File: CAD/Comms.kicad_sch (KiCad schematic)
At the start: 83 parts, among them J27 uSD_Socket, J43 USB, J46 ETHERNET, Q1 BC807, U13 MCP2542, U15 MCP2542, U16 KSZ8081RNACA, U17 74LVC2G125, U19 74LVC2G34, U3 EMIF06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

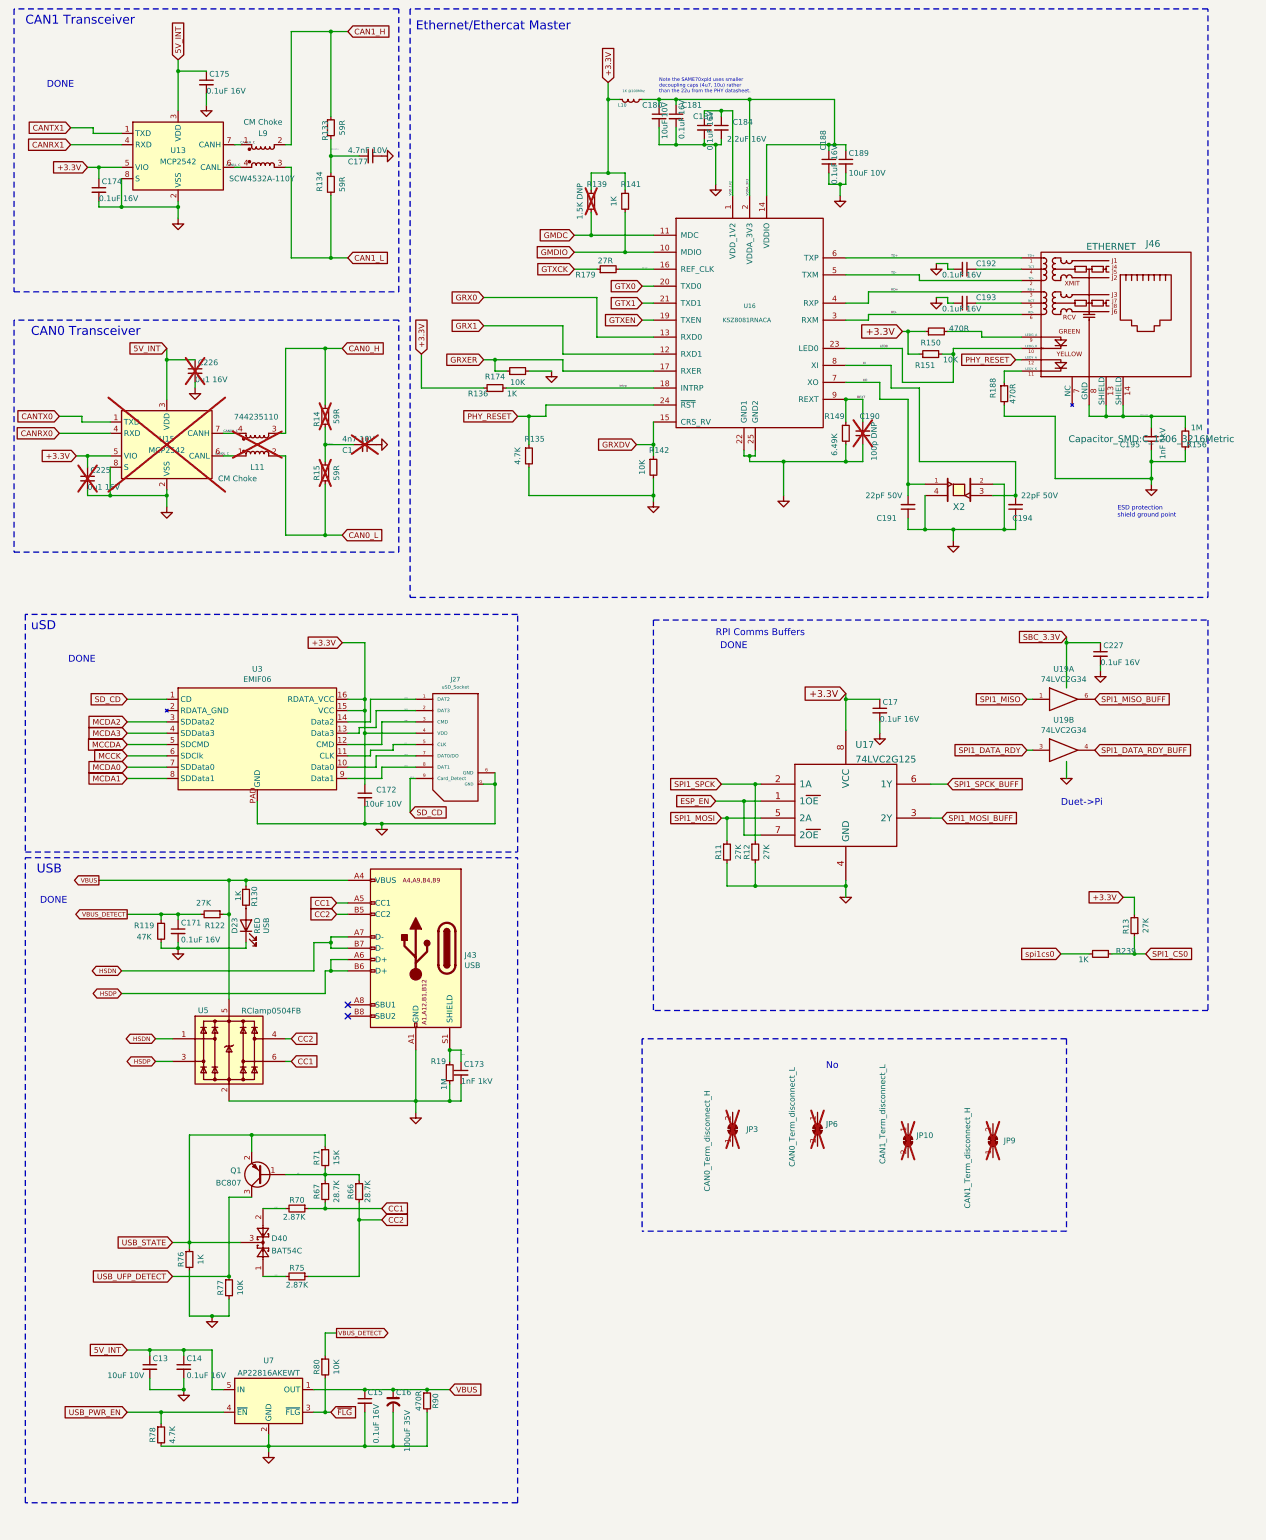
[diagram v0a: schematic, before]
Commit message: WIP redoing board for new print
Removed version resistors.
Added pull-up on CMD.
Working on motors, not routed.
Added local library for custom parts.
Ran auto-cleanup of traces and vias (supervised).
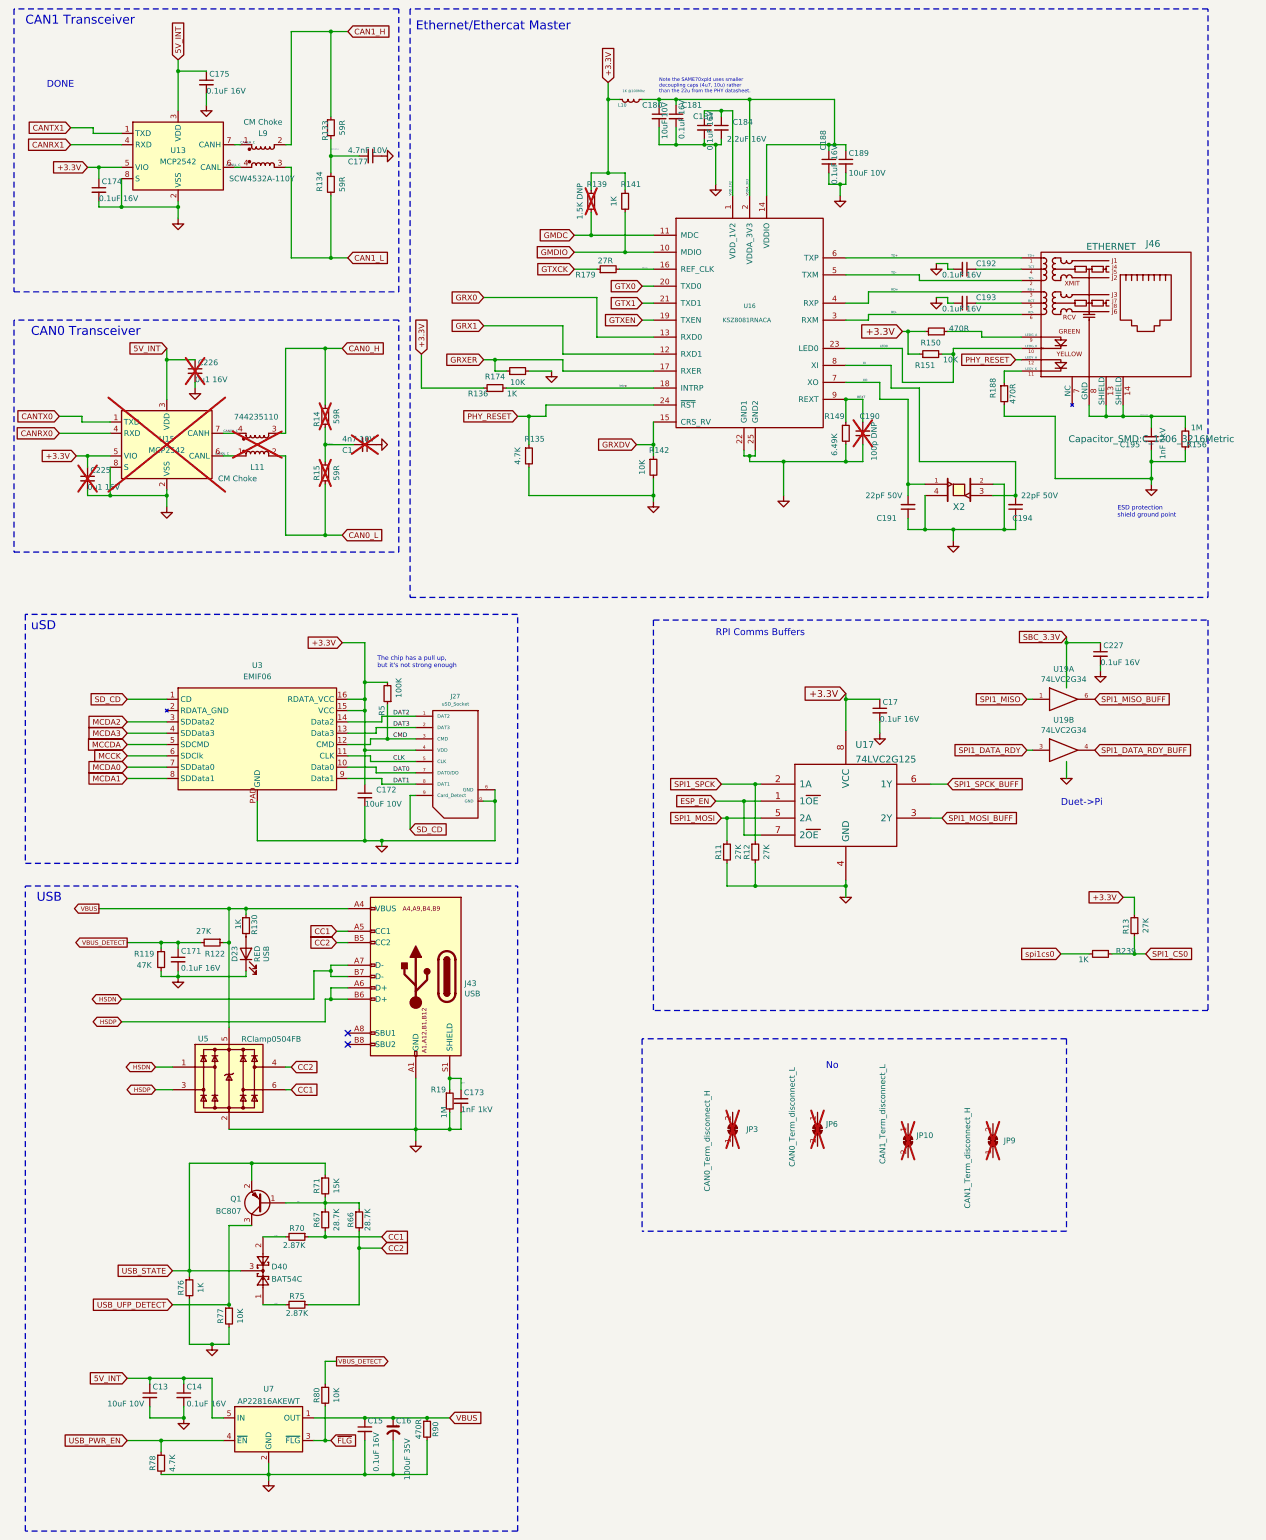
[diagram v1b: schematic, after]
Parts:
- removed U3: EMIF06, Carters_Various_Bits_and_Pieces:QFN-16L-3.5x1.2mm_P0.4mm, symbol Duet3:CM1624
- added R5: 100K, Resistor_SMD:R_0402_1005Metric, symbol Device:R_Small
- added U3: EMIF06, 3DPotter:QFN-16L-3.5x1.2mm_P0.4mm, symbol 3DPotter:EMIF06
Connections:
- net +3.3V: now also R5.2, U3.15 (VCC), U3.16 (RDATA_VCC)
- net CLK: now also U3.11 (CLK)
- net CMD: now also R5.1, U3.12 (CMD)
- net DAT0: now also U3.10 (Data0)
- net DAT1: now also U3.9 (Data1)
- net DAT2: now also U3.14 (Data2)
- net DAT3: now also U3.13 (Data3)
- net GND: now also U3.PAD (GND)
- net MCCDA: now also U3.5 (SDCMD)
- net MCCK: now also U3.6 (SDClk)
- net MCDA0: now also U3.7 (SDData0)
- net MCDA1: now also U3.8 (SDData1)
- net MCDA2: now also U3.3 (SDData2)
- net MCDA3: now also U3.4 (SDData3)
- net SD_CD: now also U3.1 (CD)
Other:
- note added: "The chip has a pull up, but it's not strong enough"
- company: Duet3d -> 3DPotter
- title: Duet 3 Main Board 6XD -> Duet 3 Main Board 3DP
- moved on the sheet: C13, C14, C15, C16, C171, C173, D23, D40, J27, J43, Q1, R119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

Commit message: update led resistors
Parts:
- R130: value 1K -> 845R; LCSC C144789 -> C227247; Part Number AC0402FR-071KL -> AC0402FR-07845RL
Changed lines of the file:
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@@
 			)
 		)
-		(property "Value" "1K"
+		(property "Value" "845R"
 			(at 65.5828 220.6752 90)
 			(effects
@@
 			)
 		)
-		(property "Part Number" "AC0402FR-071KL"
+		(property "Part Number" "AC0402FR-07845RL"
 			(at 67.31 220.98 0)
 			(effects
@@
 			)
 		)
-		(property "LCSC" "C144789"
+		(property "LCSC" "C227247"
 			(at 67.31 220.98 90)
 			(effects

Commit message: Moved Traces and Final Prep before Batch 2
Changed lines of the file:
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@@
 		)
 		(property "Footprint" "Capacitor_SMD:C_1206_3216Metric"
-			(at 270.51 111.76 0)
+			(at 270.256 114.808 0)
 			(effects
 				(font
 					(size 1.524 1.524)
 				)
+				(hide yes)
 			)
 		)

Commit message: QOL
Added a buttload of 3d models, 3d model of board is now usable. Also saved a lot of missing symbols and footprints, which are available in the 3DPotter Library.
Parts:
- J27: footprint complib:uSD_SKT -> 3DPotter:uSD_SKT; symbol Duet3:uSD_Socket -> 3DPotter:uSD_Socket
- J43: footprint complib:USB_C_Receptacle_Valcon_CSP-USC16-TR -> 3DPotter:USB_C_Receptacle_Valcon_CSP-USC16-TR; symbol Duet3:USB_C_Receptacle_USB2.0_16pin -> 3DPotter:USB_C_Receptacle_USB2.0_16pin
- J46: footprint complib:RJ45+MAG -> 3DPotter:RJ45+MAG; symbol Duet3:RJ45+MAG -> 3DPotter:RJ45+MAG
- U16: symbol Duet3:KSZ8081RNACA -> 3DPotter:KSZ8081RNACA
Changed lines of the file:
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@@
 	)
 	(symbol
-		(lib_id "Duet3:KSZ8081RNACA")
+		(lib_id "3DPotter:KSZ8081RNACA")
 		(at 180.34 86.36 0)
 		(unit 1)
@@
 	)
 	(symbol
-		(lib_id "Duet3:uSD_Socket")
+		(lib_id "3DPotter:uSD_Socket")
 		(at 113.03 185.42 0)
 		(unit 1)
@@
 			)
 		)
-		(property "Footprint" "complib:uSD_SKT"
+		(property "Footprint" "3DPotter:uSD_SKT"
 			(at 114.3 170.6626 0)
 			(effects
@@
 	)
 	(symbol
-		(lib_id "Duet3:RJ45+MAG")
+		(lib_id "3DPotter:RJ45+MAG")
 		(at 257.81 83.82 0)
 		(unit 1)
@@
 			)
 		)
-		(property "Footprint" "complib:RJ45+MAG"
+		(property "Footprint" "3DPotter:RJ45+MAG"
 			(at 280.1112 89.8398 0)
 			(effects
@@
 	)
 	(symbol
-		(lib_id "Duet3:USB_C_Receptacle_USB2.0_16pin")
+		(lib_id "3DPotter:USB_C_Receptacle_USB2.0_16pin")
 		(at 105.41 232.41 0)
 		(mirror y)
@@
 			)
 		)
-		(property "Footprint" "complib:USB_C_Receptacle_Valcon_CSP-USC16-TR"
+		(property "Footprint" "3DPotter:USB_C_Receptacle_Valcon_CSP-USC16-TR"
 			(at 101.6 232.41 0)
 			(effects

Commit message: Misc Resistor changes
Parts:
- R130: value 845R -> 5K; LCSC C227247 -> C477765; Part Number AC0402FR-07845RL -> RC0402FR-075KL
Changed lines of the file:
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@@
 			)
 		)
-		(property "Value" "845R"
+		(property "Value" "5K"
 			(at 65.5828 220.6752 90)
 			(effects
@@
 			)
 		)
-		(property "Part Number" "AC0402FR-07845RL"
+		(property "Part Number" "RC0402FR-075KL"
 			(at 67.31 220.98 0)
 			(effects
@@
 			)
 		)
-		(property "LCSC" "C227247"
+		(property "LCSC" "C477765"
 			(at 67.31 220.98 90)
 			(effects
@@
 		(dnp no)
 		(property "Reference" "R133"
-			(at 85.09 42.545 90)
-			(effects
-				(font
+			(at 84.074 42.291 90)
+			(effects
+				(font
